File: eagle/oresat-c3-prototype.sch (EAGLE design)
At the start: 93 parts, among them J1 J-SAMTEC-TFM-110-X1-XXX-D-RA, J10 2X8X1.27, J11 2X8X1.27, J12 2X8X1.27, J2 U.FL, J3 U.FL, J4 U.FL, J6 J-SAMTEC-TFM-120-X1-XXX-D-RA, J7 FTSH-105-XX-X-DV-K, J8 SD_CARD_SOCKET, J9 2X8X1.27, Q1 MOSFET-PCH-SOT23-6, Q2 MOSFET-PCH-SOT23-6, U1 MAX892LEUA+T, U2 TCAN330, U3 TCAN330, U4 TPS259621 - eFuse, U5 TPS62111RSA, U6 MAX6373KA+21-0078H-L, U7 STM32F446RE, X1 16MHZ-2.5x2mm

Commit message: I retired some of the items on the Andrew review checklist
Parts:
- removed JP6: (no value), pinhead:PINHD-1X5
- added C14: 1u, rcl_custom:C-EU0402-B-NOSILK
- added C15: 100n, rcl_custom:C-EU0402-B-NOSILK
- added C18: 100u, rcl_custom:C-EU0402-B-NOSILK
- added D6: AMBER, SparkFun-LED:LED-GREEN0603
- added R16: 10k, rcl_custom:R-US_0402-B-NOSILK
- added R18: 10k, rcl:R-US_R0402
- added R19: 10, rcl:R-US_R0402
- added TP3: TEST-POINT, Tova:TEST-POINT
- R5: value 10k -> 31.7k
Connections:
- new net N$2: C15.1, C18.1, R19.1, U6.SET1, U6.SET2, U6.VCC
- new net N$3: D6.C, R19.2
- net 3.3V: now also D6.A, R16.2, R18.1; no longer JP6.1, JP6.2, JP6.3, JP6.4, JP6.5, U6.SET1, U6.SET2, U6.VCC
- net GND: now also C14.2, C15.2, C18.2
- net MMC_PWR: now also R18.2
- net MMC_VDD: now also C14.1
- net OPD_!FAULT: now also R16.1
- net WDT: now also TP3.1
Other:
- note added: "OPD_PWR is current limited to 50mA by R36"
- note added: "Switch is off for VBUS < 5 V (undervoltage lock out)"
- note added: "VBUSP is limited to 302mA by R6"
- note added: "Watchdog"
- moved on the sheet: C1, C11, C13, C16, C17, C2, C22, C3, C6, C8, C9, D3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

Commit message: Made some changes suggested by checklist
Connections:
- removed net N$2: C15.1, C18.1, R19.1, U6.SET1, U6.SET2, U6.VCC
- new net N$4: C15.1, C18.1, R19.1, U6.SET0, U6.VCC
- net GND: now also U6.SET1, U6.SET2; no longer U6.SET0
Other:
- note added: "Internal Pull-up Resistor at MCU"

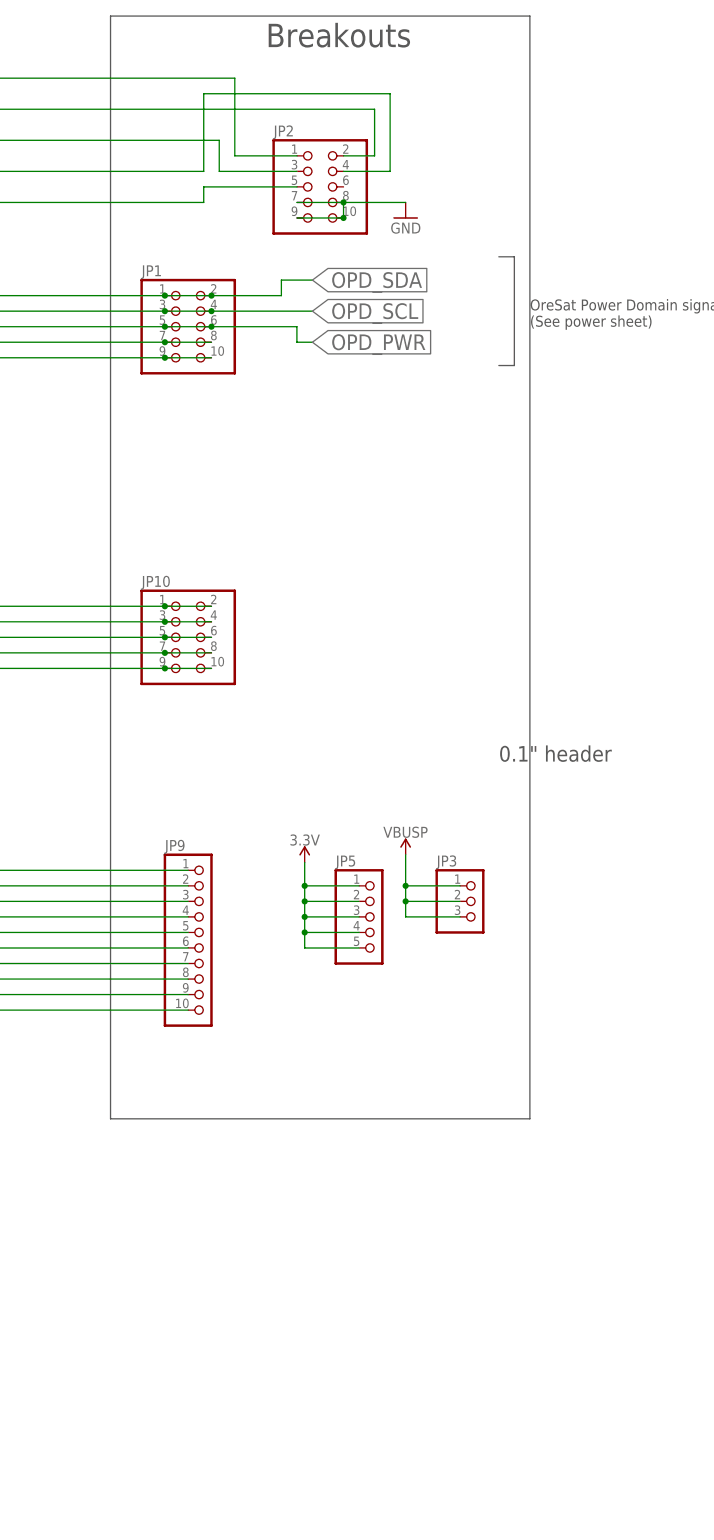
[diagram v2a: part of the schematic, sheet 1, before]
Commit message: added MCU test points
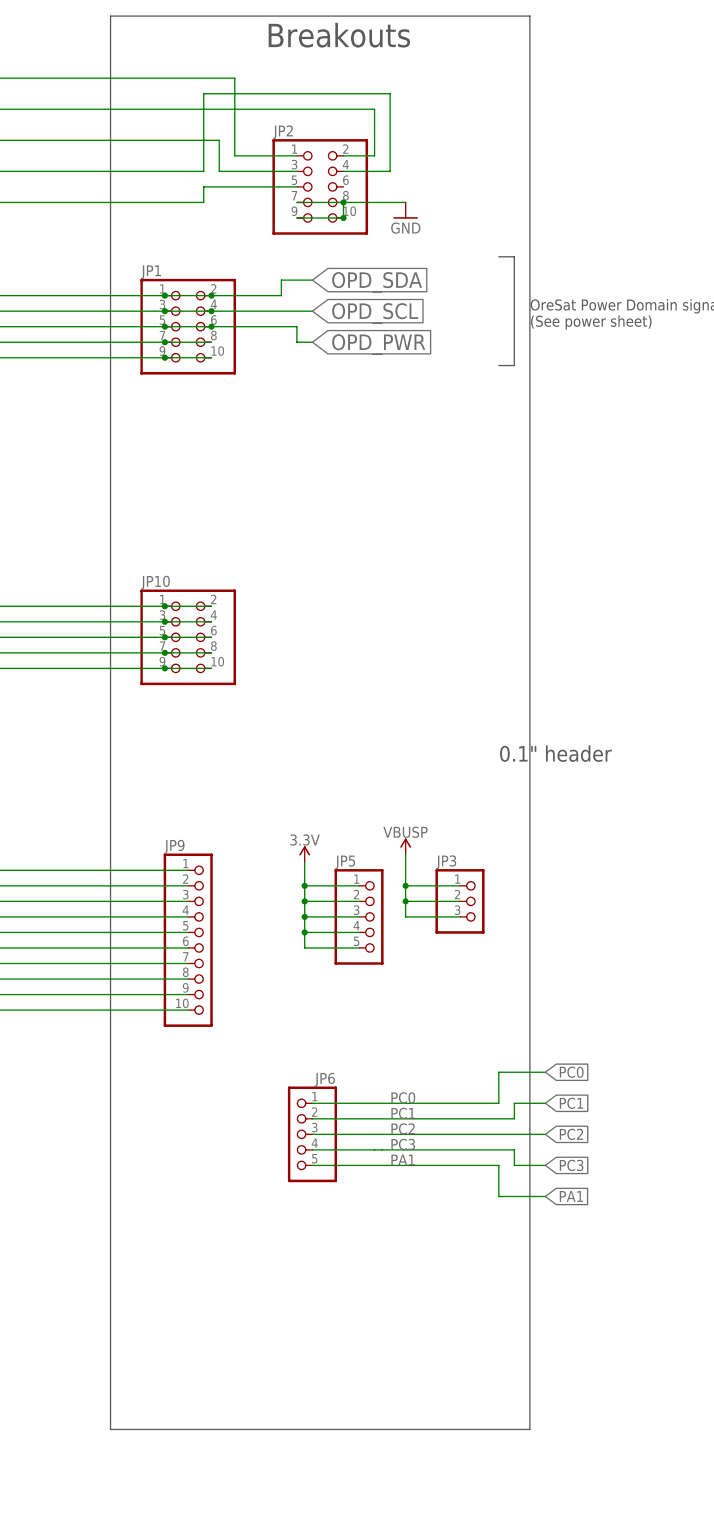
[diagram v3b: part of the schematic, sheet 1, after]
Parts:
- added JP6: (no value), pinhead:PINHD-1X5
- added TP4, TP5: TEST-POINT, Tova:TEST-POINT
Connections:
- net PA1: now also JP6.5
- net PC0: now also JP6.1
- net PC1: now also JP6.2
- net PC2: now also JP6.3
- net PC3: now also JP6.4
- net PC4: now also TP4.1
- net PC5: now also TP5.1

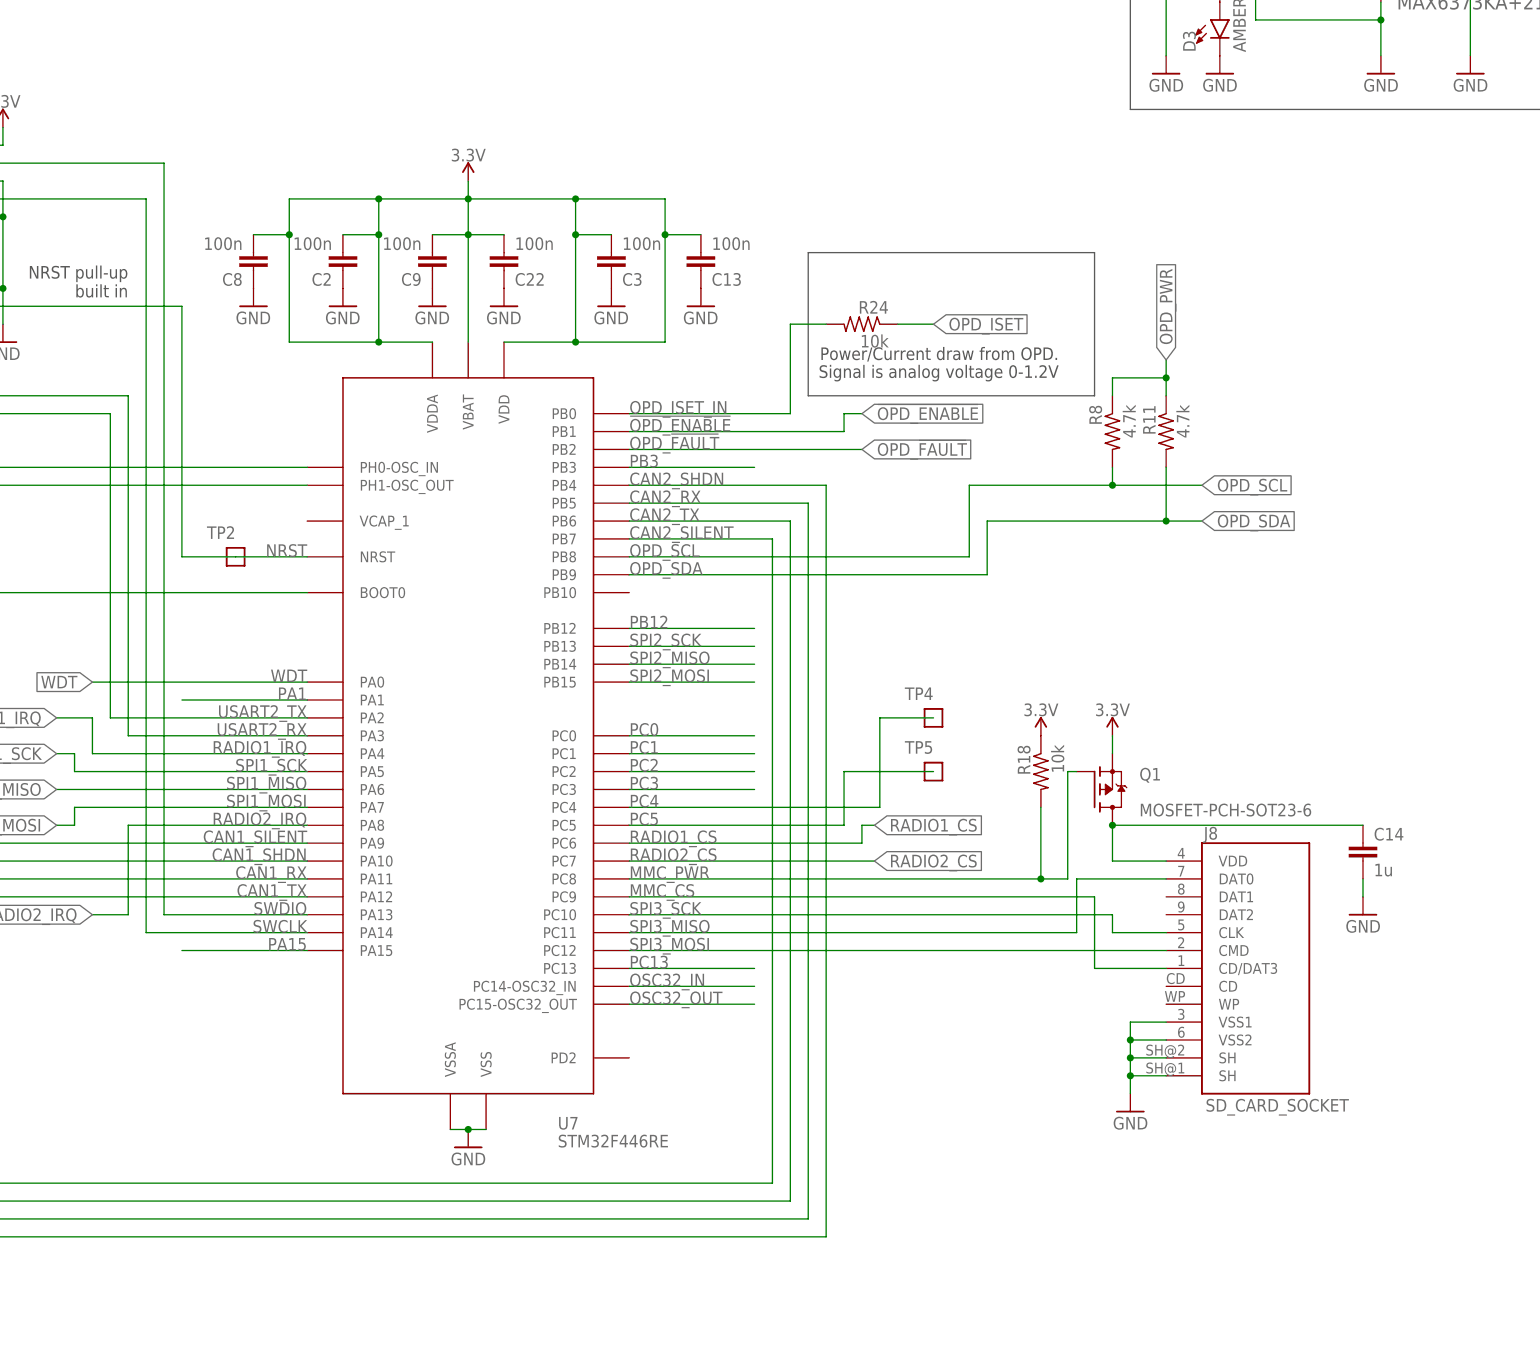
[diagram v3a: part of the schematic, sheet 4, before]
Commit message: Added some pin headers. Allocated MCU pin for analog input
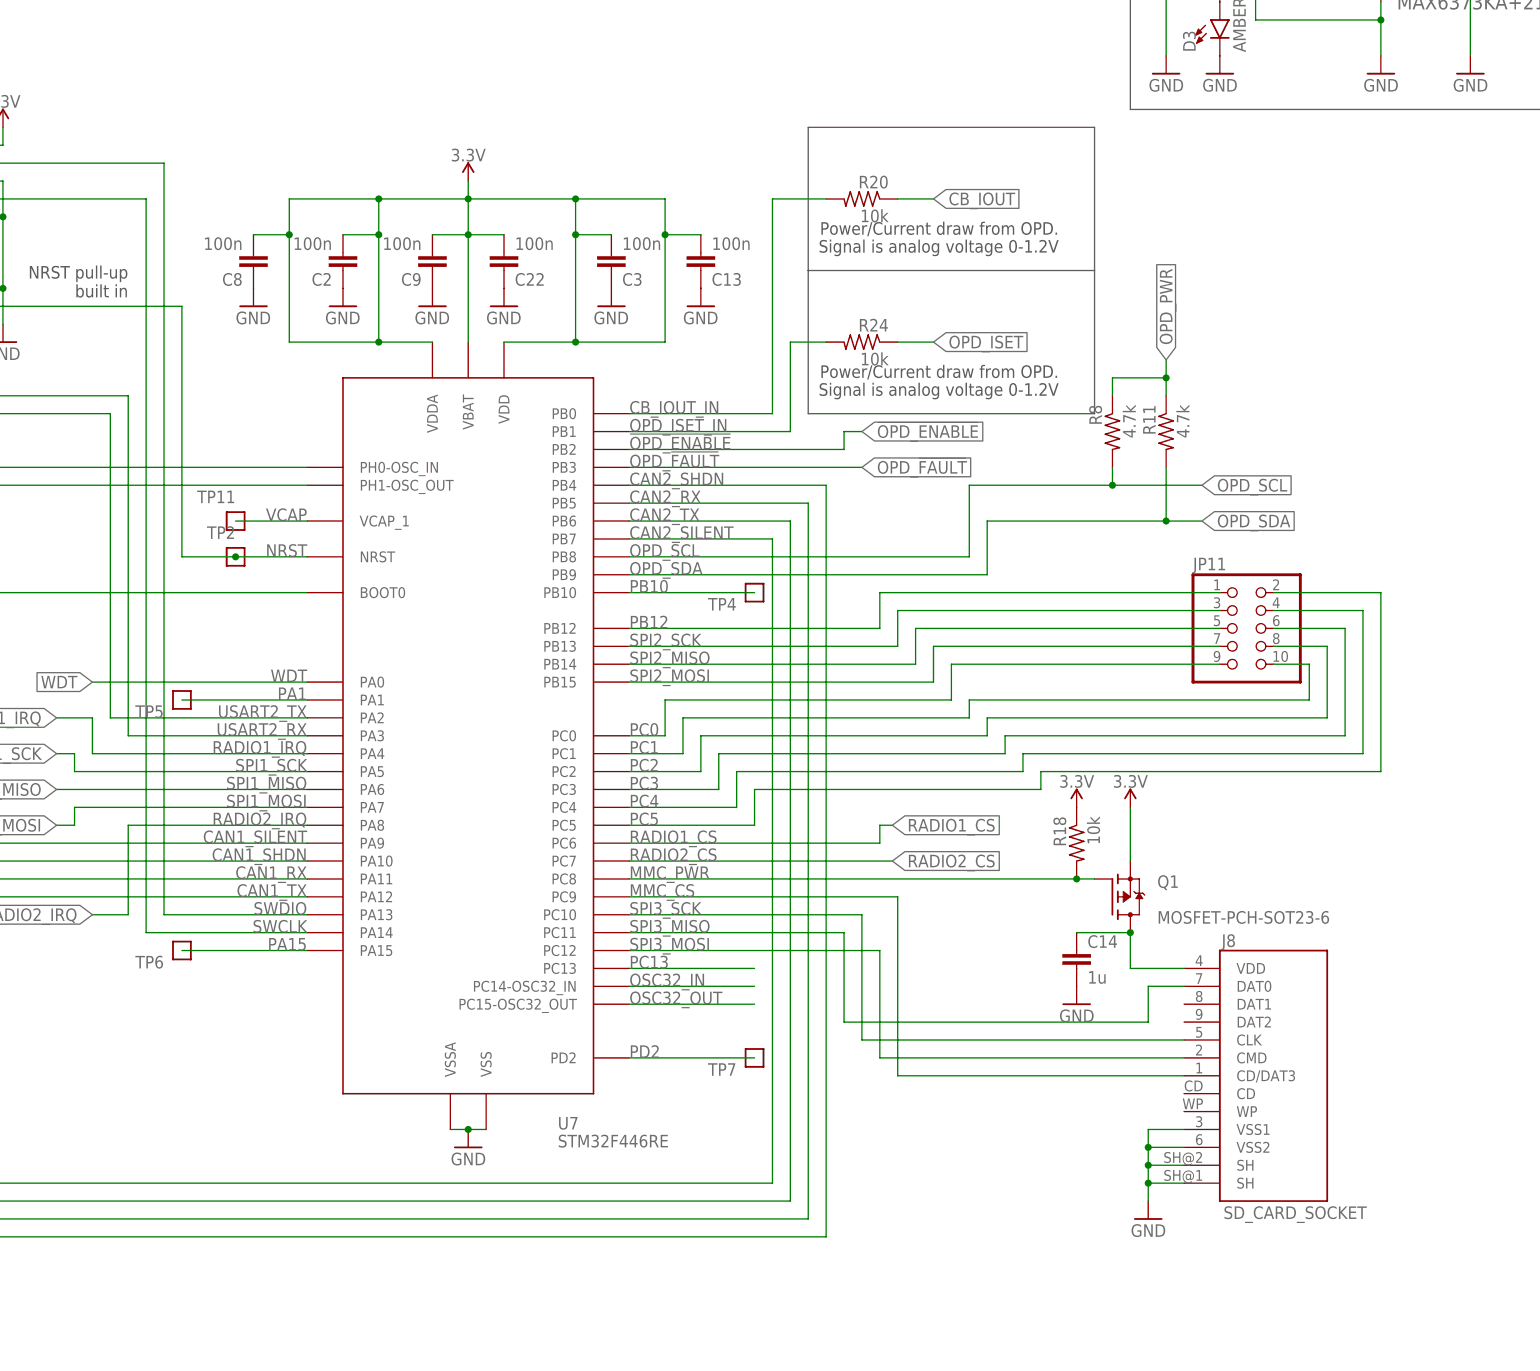
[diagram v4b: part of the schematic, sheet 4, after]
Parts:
- added JP11: (no value), pinhead:PINHD-2X5
- added R20: 10k, rcl:R-US_R0402
- added TP11, TP6, TP7: TEST-POINT, Tova:TEST-POINT
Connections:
- removed net PB3: U7.PB3
- new net CB_IOUT_IN: R20.2, U7.PB0
- new net PB10: TP4.1, U7.PB10
- new net PD2: TP7.1, U7.PD2
- new net VCAP: TP11.1, U7.VCAP_1
- net !OPD_ENABLE: now also U7.PB2; no longer U7.PB1
- net CB_IOUT: now also R20.1
- net OPD_!FAULT: now also U7.PB3; no longer U7.PB2
- net OPD_ISET_IN: now also U7.PB1; no longer U7.PB0
- net PA1: now also TP5.1
- net PA15: now also TP6.1
- net PB12: now also JP11.1
- net PC0: now also JP11.9
- net PC1: now also JP11.10
- net PC2: now also JP11.8
- net PC3: now also JP11.6
- net PC4: now also JP11.4; no longer TP4.1
- net PC5: now also JP11.2; no longer TP5.1
- net SPI2_MISO: now also JP11.5
- net SPI2_MOSI: now also JP11.7
- net SPI2_SCK: now also JP11.3
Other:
- moved on the sheet: C14, D1, J8, Q1, R1, R16, R18, R24, R4, TP4, TP5

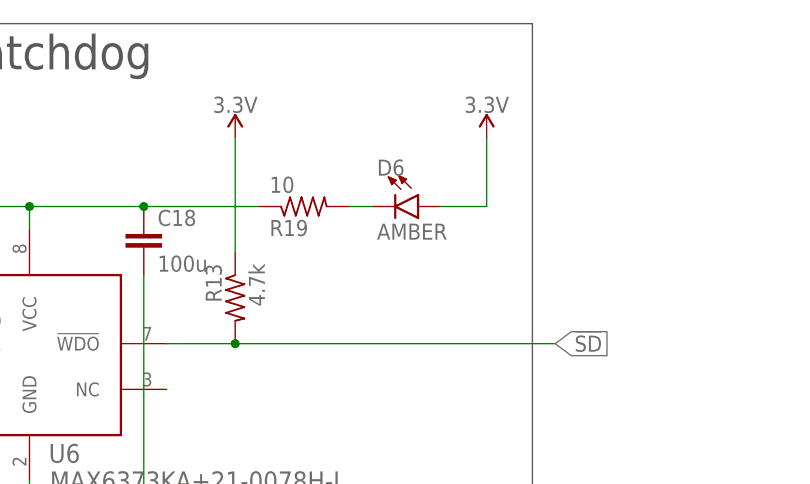
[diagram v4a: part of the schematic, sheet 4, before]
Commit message: fixed angles on jtag traces and added an WDT diode
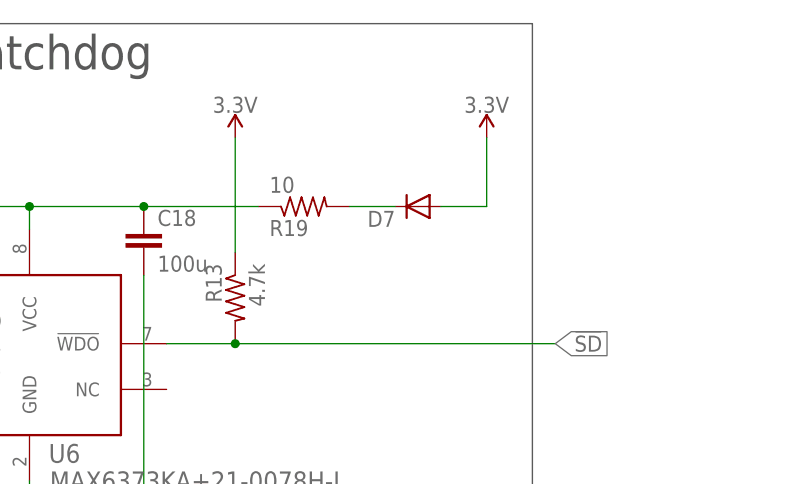
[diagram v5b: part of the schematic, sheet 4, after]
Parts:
- removed D6: AMBER, SparkFun-LED:LED-GREEN0603
- added D7: (no value), SparkFun:DIODESOD
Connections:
- net 3.3V: now also D7.A; no longer D6.A
- net N$3: now also D7.C; no longer D6.C
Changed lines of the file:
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@@
 <?xml version="1.0" encoding="utf-8"?>
 <!DOCTYPE eagle SYSTEM "eagle.dtd">
-<eagle version="9.5.2">
+<eagle version="9.5.1">
 <drawing>
 <settings>
@@
 <part name="GND54" library="supply1" library_urn="urn:adsk.eagle:library:371" deviceset="GND" device=""/>
 <part name="R19" library="rcl" library_urn="urn:adsk.eagle:library:334" deviceset="R-US_" device="R0402" package3d_urn="urn:adsk.eagle:package:23547/2" value="10"/>
-<part name="D6" library="SparkFun-LED" library_urn="urn:adsk.eagle:library:529" deviceset="LED-GREEN" device="0603" package3d_urn="urn:adsk.eagle:package:39354/1" value="AMBER"/>
 <part name="SUPPLY11" library="SparkFun-PowerSymbols" library_urn="urn:adsk.eagle:library:530" deviceset="3.3V" device=""/>
 <part name="TP3" library="Tova" deviceset="TEST-POINT" device=""/>
@@
 <part name="TP7" library="Tova" deviceset="TEST-POINT" device=""/>
 <part name="TP11" library="Tova" deviceset="TEST-POINT" device=""/>
+<part name="D7" library="SparkFun" deviceset="DIODE" device="SOD"/>
 </parts>
 <sheets>
@@
 <attribute name="VALUE" x="369.57" y="252.222" size="1.778" layer="96" rot="MR180"/>
 </instance>
-<instance part="D6" gate="G$1" x="386.08" y="248.92" smashed="yes" rot="R270">
-<attribute name="NAME" x="381.508" y="252.349" size="1.778" layer="95" font="vector"/>
-<attribute name="VALUE" x="381.508" y="247.015" size="1.778" layer="96" font="vector" align="top-left"/>
-</instance>
 <instance part="SUPPLY11" gate="G$1" x="393.7" y="256.54" smashed="yes" rot="MR0">
 <attribute name="VALUE" x="393.7" y="259.334" size="1.778" layer="96" rot="MR0" align="bottom-center"/>
@@
 <attribute name="NAME" x="180.34" y="147.32" size="1.778" layer="95" font="vector" rot="MR0"/>
 </instance>
+<instance part="D7" gate="G$1" x="386.08" y="248.92" smashed="yes" rot="R180">
+<attribute name="NAME" x="383.54" y="248.4374" size="1.778" layer="95" rot="R180"/>
+<attribute name="VALUE" x="383.54" y="251.2314" size="1.778" layer="96" rot="R180"/>
+</instance>
 </instances>
 <busses>
@@
 <wire x1="393.7" y1="256.54" x2="393.7" y2="248.92" width="0.1524" layer="91"/>
 <wire x1="388.62" y1="248.92" x2="393.7" y2="248.92" width="0.1524" layer="91"/>
-<pinref part="D6" gate="G$1" pin="A"/>
+<pinref part="D7" gate="G$1" pin="A"/>
 </segment>
 </net>
@@
 <segment>
 <pinref part="R19" gate="G$1" pin="2"/>
-<pinref part="D6" gate="G$1" pin="C"/>
-<wire x1="378.46" y1="248.92" x2="381" y2="248.92" width="0.1524" layer="91"/>
+<wire x1="383.54" y1="248.92" x2="378.46" y2="248.92" width="0.1524" layer="91"/>
+<pinref part="D7" gate="G$1" pin="C"/>
 </segment>
 </net>
